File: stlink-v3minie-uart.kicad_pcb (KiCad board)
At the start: 2 copper layers, 0 parts

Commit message: pcb: import footprints from schem
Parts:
- added J1: Conn_01x05, Connector_PinHeader_2.54mm:PinHeader_1x05_P2.54mm_Horizontal, F.Cu at (145.3, 96.5)
- added J2: Conn_02x05_Top_Bottom, GLCS:KYOCERA_AVX9159-006, F.Cu at (151.5, 109.8)
- added J3: Conn_01x04_Pin, Connector_PinHeader_2.54mm:PinHeader_1x04_P2.54mm_Vertical, F.Cu at (158.7, 96.5)
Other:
- board outline added: 10 x 3 mm

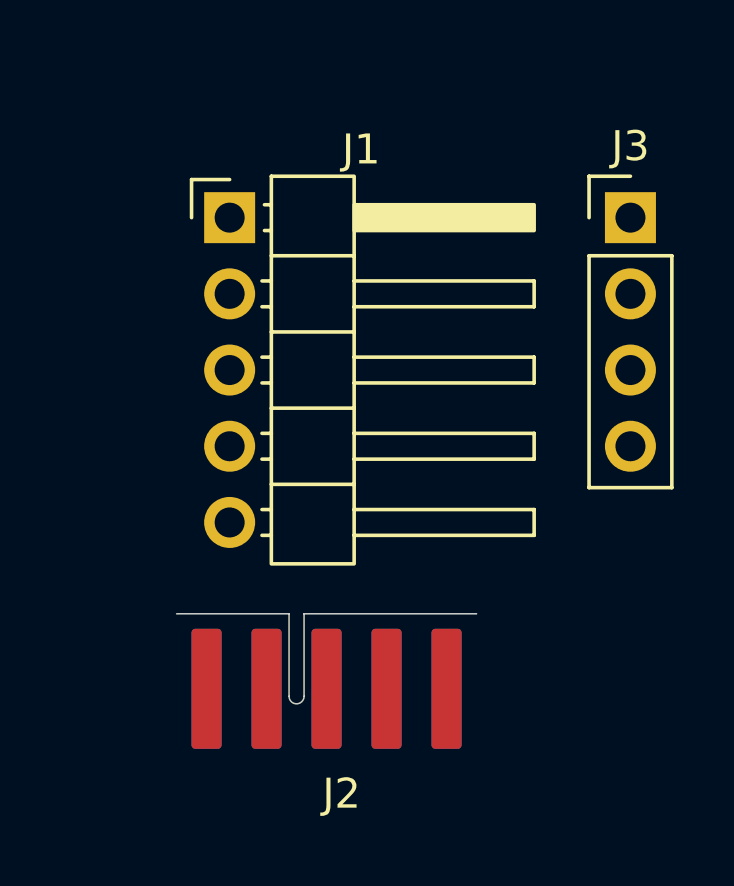
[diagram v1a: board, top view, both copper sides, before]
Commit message: pcb: initial rough placement
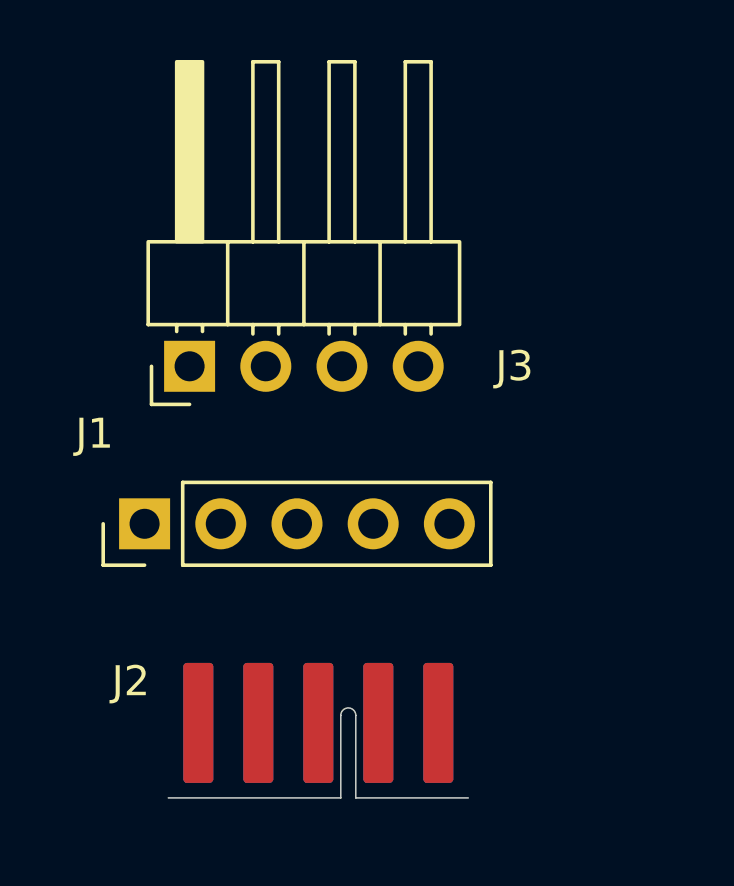
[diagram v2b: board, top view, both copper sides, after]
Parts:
- J1: footprint Connector_PinHeader_2.54mm:PinHeader_1x05_P2.54mm_Horizontal -> Connector_PinHeader_2.54mm:PinHeader_1x05_P2.54mm_Vertical
- J3: footprint Connector_PinHeader_2.54mm:PinHeader_1x04_P2.54mm_Vertical -> Connector_PinHeader_2.54mm:PinHeader_1x04_P2.54mm_Horizontal
- moved J3 15.5 mm to (144.0, 101.5), turned to 90 degrees
- moved J1 10.6 mm to (142.5, 106.8), turned to 90 degrees
- moved J2 8.78 mm to (145.2, 115.9), turned to 180 degrees
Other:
- outline, holes or cut-outs redrawn

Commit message: pcb: oui
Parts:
- moved J3 3.14 mm to (146.4, 103.5)
- moved J1 2.66 mm to (144.9, 107.8)
- moved J2 1.75 mm to (147.0, 116.0)
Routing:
- added copper zone on B.Cu, net GND
- added copper zone on F.Cu, net GND
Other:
- board size 10 x 3 mm -> 14 x 23 mm
- board text added: "+"
- board text added: "-"
- board text added: "CLK"
- board text added: "D"
- board text added: "JTDI"
- board text added: "O"
- board text added: "R"
- board text added: "RX"
- board text added: "TX"
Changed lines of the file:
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@@
 	(footprint "GLCS:KYOCERA_AVX9159-006"
 		(layer "F.Cu")
-		(at 145.25 115.8875 180)
+		(at 147 116 180)
 		(descr "board to board 10 pin edge connector https://www.kyocera-avx.com/download/connectors/Conn-Sales-Drawings/9XXX/9159-06X.zip")
 		(tags "edge b2b")
 		(property "Reference" "J2"
-			(at 3.25 3.8875 0)
+			(at 2.75 3.25 0)
 			(layer "F.SilkS")
 			(effects
@@
 	(footprint "Connector_PinHeader_2.54mm:PinHeader_1x05_P2.54mm_Vertical"
 		(layer "F.Cu")
-		(at 142.46 106.75 90)
+		(at 144.92 107.75 90)
 		(descr "Through hole straight pin header, 1x05, 2.54mm pitch, single row")
 		(tags "Through hole pin header THT 1x05 2.54mm single row")
 		(property "Reference" "J1"
-			(at 3 -1.67 180)
+			(at 2.5 -0.67 180)
 			(layer "F.SilkS")
 			(effects
@@
 	(footprint "Connector_PinHeader_2.54mm:PinHeader_1x04_P2.54mm_Horizontal"
 		(layer "F.Cu")
-		(at 143.96 101.5 90)
+		(at 146.38 103.5 90)
 		(descr "Through hole angled pin header, 1x04, 2.54mm pitch, 6mm pin length, single row")
 		(tags "Through hole angled pin header THT 1x04 2.54mm single row")
 		(property "Reference" "J3"
-			(at 0 10.83 180)
+			(at 7.5 9.62 180)
 			(layer "F.SilkS")
 			(effects
@@
 			)
 		)
+	)
+	(gr_arc
+		(start 143 95)
+		(mid 143.585786 93.585786)
+		(end 145 93)
+		(stroke
+			(width 0.05)
+			(type default)
+		)
+		(layer "Edge.Cuts")
+	)
+	(gr_line
+		(start 143 114)
+		(end 143 95)
+		(stroke
+			(width 0.05)
+			(type default)
+		)
+		(layer "Edge.Cuts")
+	)
+	(gr_arc
+		(start 145 116)
+		(mid 143.585786 115.414214)
+		(end 143 114)
+		(stroke
+			(width 0.05)
+			(type default)
+		)
+		(layer "Edge.Cuts")
+	)
+	(gr_line
+		(start 155 93)
+		(end 145 93)
+		(stroke
+			(width 0.05)
+			(type default)
+		)
+		(layer "Edge.Cuts")
+	)
+	(gr_arc
+		(start 155 93)
+		(mid 156.414214 93.585786)
+		(end 157 95)
+		(stroke
+			(width 0.05)
+			(type default)
+		)
+		(layer "Edge.Cuts")
+	)
+	(gr_arc
+		(start 157 114)
+		(mid 156.414214 115.414214)
+		(end 155 116)
+		(stroke
+			(width 0.05)
+			(type default)
+		)
+		(layer "Edge.Cuts")
+	)
+	(gr_line
+		(start 157 114)
+		(end 157 95)
+		(stroke
+			(width 0.05)
+			(type default)
+		)
+		(layer "Edge.Cuts")
+	)
+	(gr_text "O"
+		(at 144.25 111 0)
+		(layer "F.SilkS" knockout)
+		(effects
+			(font
+				(size 1 1)
+				(thickness 0.2)
+				(bold yes)
+			)
+			(justify left bottom)
+		)
+	)
+	(gr_text "+"
+		(at 145.628589 106.012058 0)
+		(layer "F.SilkS" knockout)
+		(effects
+			(font
+				(size 1 1)
+				(thickness 0.2)
+				(bold yes)
+			)
+			(justify left bottom)
+		)
+	)
+	(gr_text "CLK"
+		(at 145.75 111 0)
+		(layer "F.SilkS" knockout)
+		(effects
+			(font
+				(size 1 1)
+				(thickness 0.2)
+				(bold yes)
+			)
+			(justify left bottom)
+		)
+	)
+	(gr_text "TX"
+		(at 148 106 0)
+		(layer "F.SilkS" knockout)
+		(effects
+			(font
+				(size 1 1)
+				(thickness 0.2)
+				(bold yes)
+			)
+			(justify left bottom)
+		)
+	)
+	(gr_text "D"
+		(at 149.25 111 0)
+		(layer "F.SilkS" knockout)
+		(effects
+			(font
+				(size 1 1)
+				(thickness 0.2)
+				(bold yes)
+			)
+			(justify left bottom)
+		)
+	)
+	(gr_text "-"
+		(at 150.67177 105.750075 0)
+		(layer "F.SilkS" knockout)
+		(effects
+			(font
+				(size 1 1)
+				(thickness 0.2)
+				(bold yes)
+			)
+			(justify left bottom)
+		)
+	)
+	(gr_text "JTDI"
+		(at 151 111 0)
+		(layer "F.SilkS" knockout)
+		(effects
+			(font
+				(size 1 1)
+				(thickness 0.2)
+				(bold yes)
+			)
+			(justify left bottom)
+		)
+	)
+	(gr_text "RX"
+		(at 152.922445 106.00015 0)
+		(layer "F.SilkS" knockout)
+		(effects
+			(font
+				(size 1 1)
+				(thickness 0.2)
+				(bold yes)
+			)
+			(justify left bottom)
+		)
+	)
+	(gr_text "R"
+		(at 154.5 111 0)
+		(layer "F.SilkS" knockout)
+		(effects
+			(font
+				(size 1 1)
+				(thickness 0.2)
+				(bold yes)
+			)
+			(justify left bottom)
+		)
+	)
+	(zone
+		(net "GND")
+		(layers "F.Cu" "B.Cu")
+		(hatch edge 0.5)
+		(connect_pads
+			(clearance 0.2)
+		)
+		(min_thickness 0.15)
+		(fill yes
+			(thermal_gap 0.35)
+			(thermal_bridge_width 0.35)
+			(island_removal_mode 0)
+		)
+		(polygon
+			(pts
+				(xy 143 93) (xy 143 116) (xy 157 116) (xy 157 93)
+			)
+		)
